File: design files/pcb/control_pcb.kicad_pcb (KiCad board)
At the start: 2 copper layers, 19.8 x 99.3 mm, 23 parts, among them J1 P1_CV, J2 MODE_CV, J5 GAIN_CV, J6 OUT, J7 HDR-M-2.54_1x9, P1_POT 10-100k, P2_POT 10-100k, U4 TOGGLE SWITCH SPDT

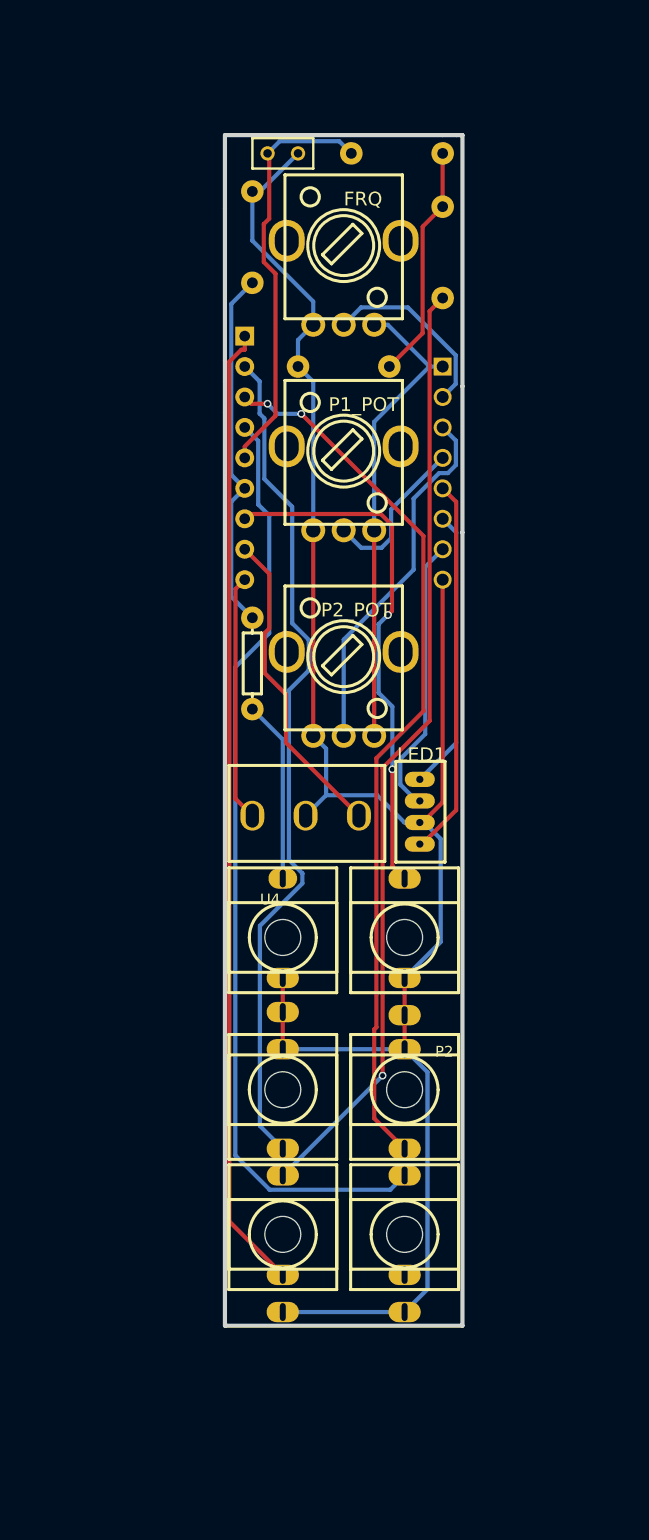
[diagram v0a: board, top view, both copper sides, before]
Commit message: revision 1.1 pcb
mainly better footprints, slightly more space for the power adapter
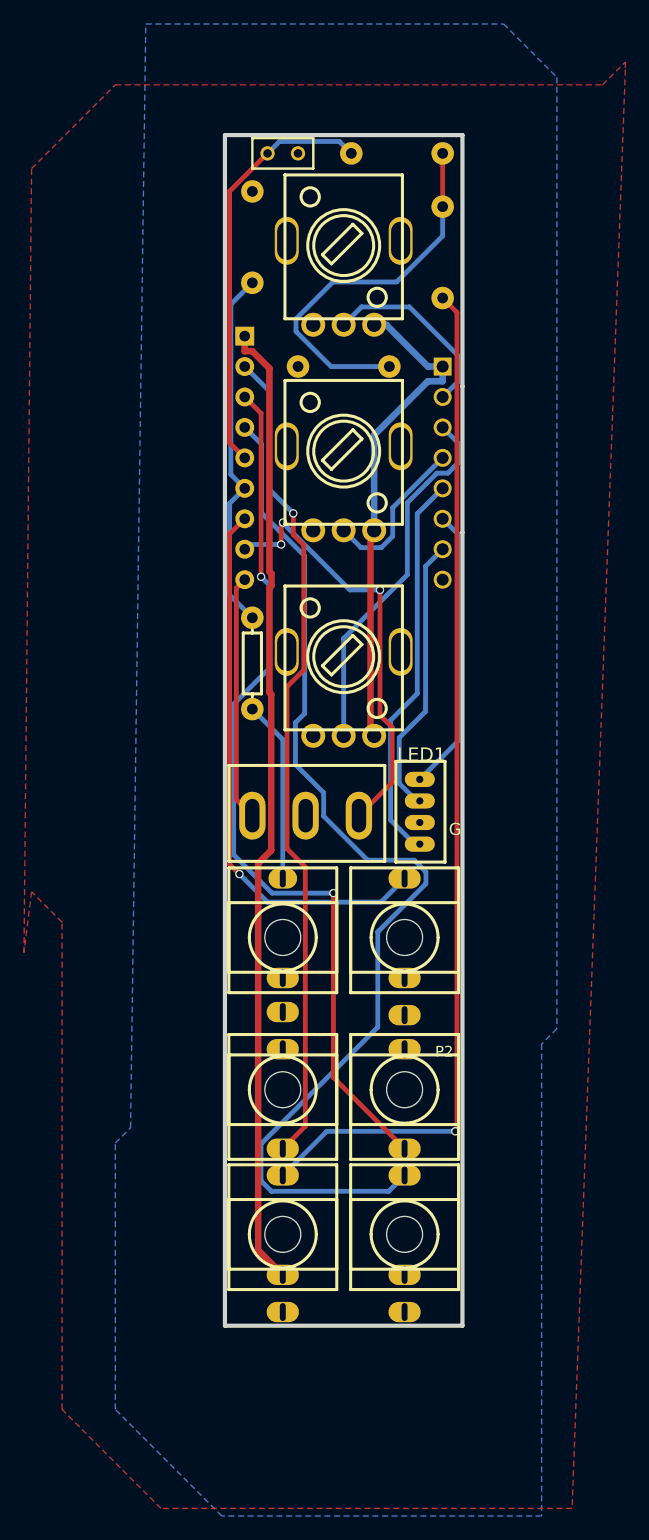
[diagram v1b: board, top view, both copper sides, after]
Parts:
- removed C14: 100n, easyeda:RAD-0.1
- removed H3: Header-Male-2.54_1x8, easyeda:HDR-TH_8P-P2.54-V-M
- removed J5: GAIN_CV, easyeda:THONKICONN_1
- removed J6: OUT, easyeda:THONKICONN_1
- added C12: 100n, easyeda:RAD-0.1, F.Cu at (9.53, 115.2)
- added H2: Header-Male-2.54_1x8, easyeda:HDR-TH_8P-P2.54-V-M, F.Cu at (22.9, 141.9)
- added J3: MODE_CV, easyeda:THONKICONN_1, F.Cu at (19.7, 180.6)
- added J8: OUT, easyeda:THONKICONN_1, F.Cu at (19.7, 205.4)
- J1: value P1_CV -> HDR-M-2.54_1x9; footprint easyeda:THONKICONN_1 -> easyeda:HDR-M-2.54_1X9
- J2: value MODE_CV -> P1_CV
- J7: value HDR-M-2.54_1x9 -> GAIN_CV; footprint easyeda:HDR-M-2.54_1X9 -> easyeda:THONKICONN_1
- moved J7 64.8 mm to (9.53, 205.4), turned to 0 degrees
- moved J1 52.8 mm to (6.35, 140.6), turned to 90 degrees
- moved J2 16.3 mm to (9.53, 193.3), turned to 180 degrees
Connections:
- ? pad 3: J4_3 -> J5_3
- J1 pad 1: GND -> +12V
- J1 pad 2: GND -> P1CV
- J1 pad 3: P1CV -> P2CV
- J2 pad 3: MODECV -> P1CV
- J7 pad 1: +12V -> GND
- J7 pad 2: P1CV -> +12V
- J7 pad 3: P2CV -> J7_3
- R12 pad 2: J4_3 -> J5_3
- R14 pad 2: J5_3 -> J7_3
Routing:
- net GND: track 162.3 -> 0.00 mm
- net J7_3: track 0.00 -> 86.0 mm, vias 0 -> 1
- net J5_3: track 78.7 -> 15.2 mm, vias 1 -> 0
- net J4_3: track 15.2 -> 0.00 mm
- net R14_1: track 19.6 -> 32.0 mm
- net OUT: track 78.6 -> 90.6 mm
- net SW1: track 26.5 -> 36.0 mm, vias 0 -> 3
- net MODECV: track 43.7 -> 46.1 mm, vias 2 -> 1
- net P1CV: track 70.9 -> 69.3 mm, vias 0 -> 1
- net +5V: track 39.9 -> 41.3 mm
- net LED1: track 31.5 -> 32.7 mm
- added copper zone on B.Cu, net GND
- added copper zone on F.Cu, net GND
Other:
- board text added: "Circuit by HAGIWO, PCB by Testbild"
- board text added: "G"
- board text added: "Revision 1.1"
- board text added: "Testbild/Hagiwo Arduino OSC"
